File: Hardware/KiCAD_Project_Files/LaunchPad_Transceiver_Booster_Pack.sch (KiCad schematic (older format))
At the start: 24 parts, among them P1 CONN_10, P10 CONN_1, P2 CONN_10, P3 CONN_2, P4 CONN_3, P5 CONN_2X2, P6 CONN_3, P7 HOPERF_RFM22, P8 CONN_4, P9 CONN_6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

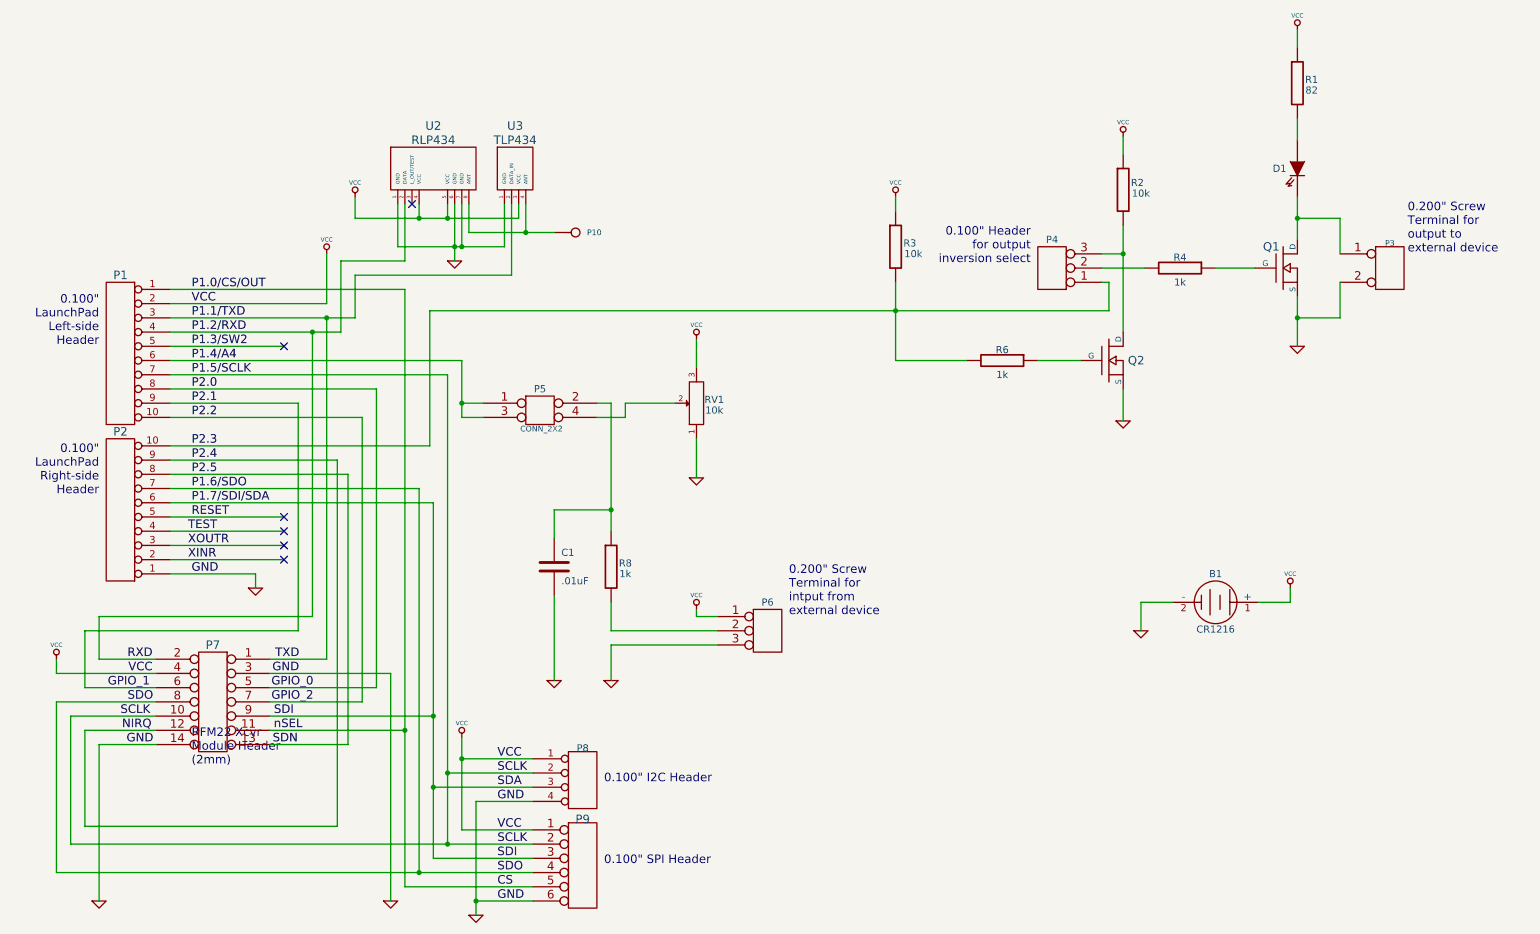
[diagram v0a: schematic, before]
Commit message: Added BOM file Fixed many of the PCB footprints by re-linking the 3D part Fixed P1 connections by swapping pins 1 and 2 Reprinted schematic to reflect P1 changes
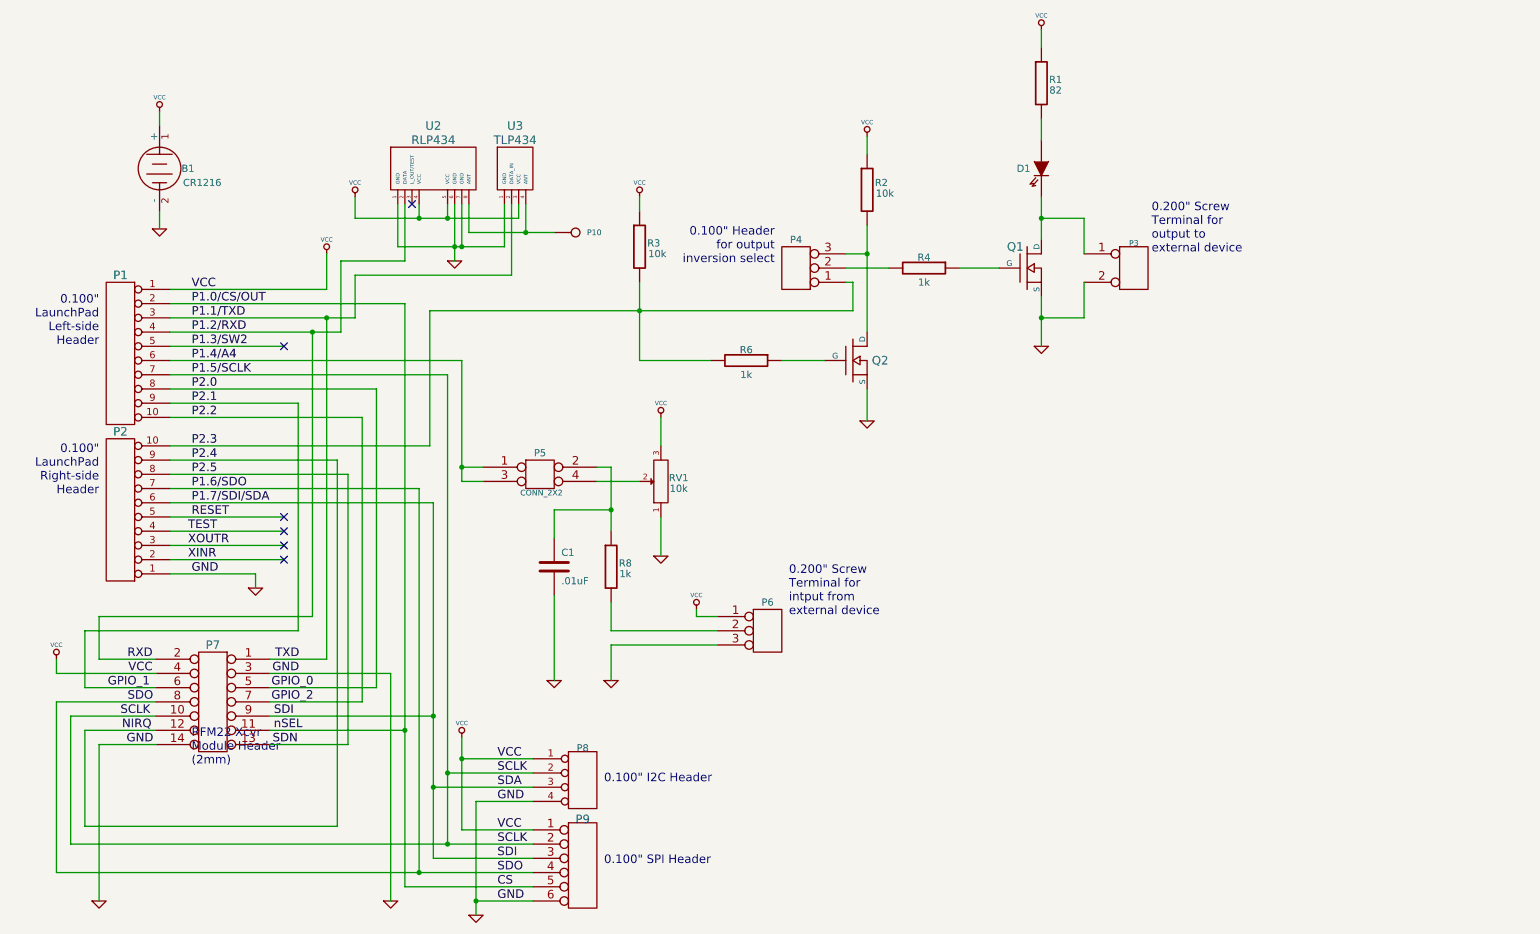
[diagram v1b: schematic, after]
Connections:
- net CS: now also P1.2 (P2); no longer P1.1 (P1)
- net VCC: now also P1.1 (P1); no longer P1.2 (P2)
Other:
- moved on the sheet: B1, D1, P3, P4, P5, Q1, Q2, R1, R2, R3, R4, R6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
